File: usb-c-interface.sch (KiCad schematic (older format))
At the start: 62 parts, among them IC3 TPS7A0518PDBVT, J11 12401598E4_2A, J3 12401598E4_2A, J4 12401598E4_2A, U5 TPS25820DSST, U6 NX3DV42GU, U7 TXB0104RUT, U8 CBTL02043ABQ,115, U9 FT232RQ-REEL

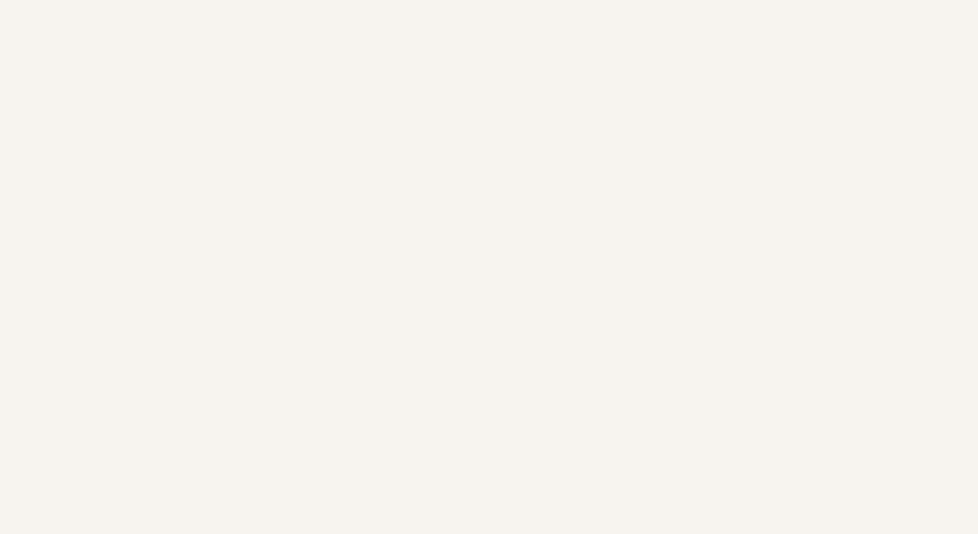
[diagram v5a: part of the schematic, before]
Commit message: Add EDS for host USB-C
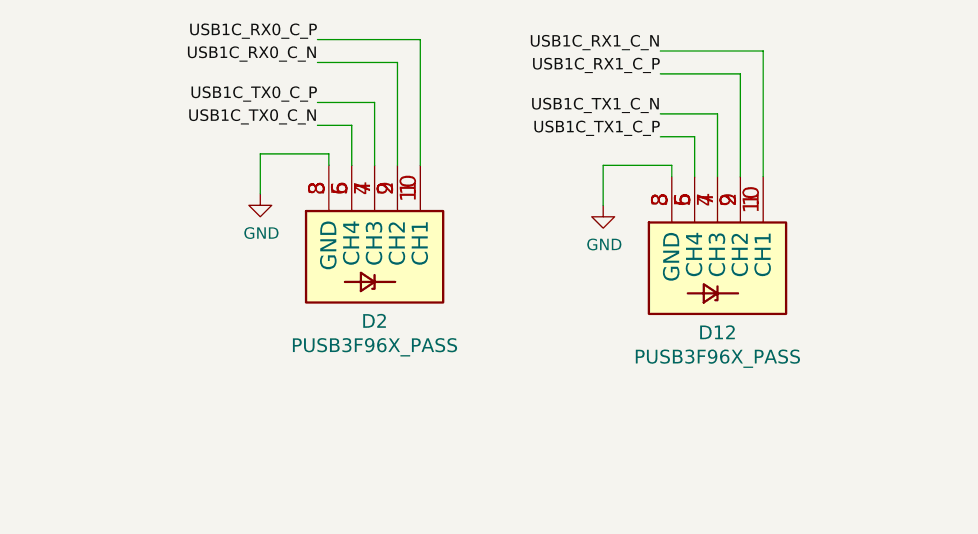
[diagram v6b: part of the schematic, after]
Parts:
- added D12, D2: PUSB3F96X_PASS, sa800u-baseboard-hw-footprints:PUSB3F96X, symbol sa800u-baseboard-hw:PUSB3F96X_PASS
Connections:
- net GND: now also D12.3 (GND), D12.8 (GND), D2.3 (GND), D2.8 (GND)
- net USB1C_RX0_C_N: now also D2.2 (CH2), D2.9 (CH2)
- net USB1C_RX0_C_P: now also D2.1 (CH1), D2.10 (CH1)
- net USB1C_RX1_C_N: now also D12.1 (CH1), D12.10 (CH1)
- net USB1C_RX1_C_P: now also D12.2 (CH2), D12.9 (CH2)
- net USB1C_TX0_C_N: now also D2.5 (CH4), D2.6 (CH4)
- net USB1C_TX0_C_P: now also D2.4 (CH3), D2.7 (CH3)
- net USB1C_TX1_C_N: now also D12.4 (CH3), D12.7 (CH3)
- net USB1C_TX1_C_P: now also D12.5 (CH4), D12.6 (CH4)
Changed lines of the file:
@@
 Text GLabel 1150 9550 0    50   Input ~ 0
 USB2_SS_RX_P
+Wire Wire Line
+	9175 -1675 9175 -1725
+Wire Wire Line
+	8875 -1725 8875 -1550
+$Comp
+L sa800u-baseboard-hw:GND #PWR?
+U 1 1 6217AF63
+P 8875 -1550
+AR Path="/61A60486/6217AF63" Ref="#PWR?"  Part="1"
+AR Path="/61C01D88/6217AF63" Ref="#PWR?"  Part="1"
+AR Path="/61A2F307/6217AF63" Ref="#PWR0257"  Part="1"
+F 0 "#PWR0257" H 8875 -1800 50  0001 C CNN
+F 1 "GND" H 8880 -1723 50  0000 C CNN
+F 2 "" H 8875 -1550 50  0001 C CNN
+F 3 "" H 8875 -1550 50  0001 C CNN
+	1    8875 -1550
+	1    0    0    -1
+$EndComp
+Wire Wire Line
+	9125 -1850 9275 -1850
+Wire Wire Line
+	9275 -1850 9275 -1675
+Wire Wire Line
+	9125 -1950 9375 -1950
+Wire Wire Line
+	9375 -1950 9375 -1675
+Wire Wire Line
+	9475 -1675 9475 -2125
+Wire Wire Line
+	9575 -1675 9575 -2225
+Wire Wire Line
+	8875 -1725 9175 -1725
+$Comp
+L sa800u-baseboard-hw:PUSB3F96X_PASS D?
+U 1 1 6217AF74
+P 9375 -1475
+AR Path="/6197686D/6217AF74" Ref="D?"  Part="1"
+AR Path="/61A2F307/6217AF74" Ref="D12"  Part="1"
+F 0 "D12" V 9858 -1475 60  0000 C CNN
+F 1 "PUSB3F96X_PASS" V 9964 -1475 60  0000 C CNN
+F 2 "sa800u-baseboard-hw-footprints:PUSB3F96X" H 9575 -2025 60  0001 C CNN
+F 3 "https://pl.mouser.com/datasheet/2/916/PUSB3F96-1600324.pdf" H 9375 -1475 60  0001 C CNN
+F 4 "Nexperia" H 9575 -2125 50  0001 C CNN "Manufacturer"
+F 5 "PUSB3F96X" H 9575 -2125 50  0001 C CNN "MPN"
+	1    9375 -1475
+	0    1    1    0
+$EndComp
+Wire Wire Line
+	7675 -1725 7675 -1775
+Wire Wire Line
+	7375 -1775 7375 -1600
+$Comp
+L sa800u-baseboard-hw:GND #PWR?
+U 1 1 621C0750
+P 7375 -1600
+AR Path="/61A60486/621C0750" Ref="#PWR?"  Part="1"
+AR Path="/61C01D88/621C0750" Ref="#PWR?"  Part="1"
+AR Path="/61A2F307/621C0750" Ref="#PWR0265"  Part="1"
+F 0 "#PWR0265" H 7375 -1850 50  0001 C CNN
+F 1 "GND" H 7380 -1773 50  0000 C CNN
+F 2 "" H 7375 -1600 50  0001 C CNN
+F 3 "" H 7375 -1600 50  0001 C CNN
+	1    7375 -1600
+	1    0    0    -1
+$EndComp
+Wire Wire Line
+	7625 -1900 7775 -1900
+Wire Wire Line
+	7775 -1900 7775 -1725
+Wire Wire Line
+	7625 -2000 7875 -2000
+Wire Wire Line
+	7875 -2000 7875 -1725
+Wire Wire Line
+	7975 -1725 7975 -2175
+Wire Wire Line
+	7625 -2175 7975 -2175
+Wire Wire Line
+	8075 -1725 8075 -2275
+Wire Wire Line
+	7625 -2275 8075 -2275
+Wire Wire Line
+	7375 -1775 7675 -1775
+$Comp
+L sa800u-baseboard-hw:PUSB3F96X_PASS D?
+U 1 1 621C0761
+P 7875 -1525
+AR Path="/6197686D/621C0761" Ref="D?"  Part="1"
+AR Path="/61A2F307/621C0761" Ref="D2"  Part="1"
+F 0 "D2" V 8358 -1525 60  0000 C CNN
+F 1 "PUSB3F96X_PASS" V 8464 -1525 60  0000 C CNN
+F 2 "sa800u-baseboard-hw-footprints:PUSB3F96X" H 8075 -2075 60  0001 C CNN
+F 3 "https://pl.mouser.com/datasheet/2/916/PUSB3F96-1600324.pdf" H 7875 -1525 60  0001 C CNN
+F 4 "Nexperia" H 8075 -2175 50  0001 C CNN "Manufacturer"
+F 5 "PUSB3F96X" H 8075 -2175 50  0001 C CNN "MPN"
+	1    7875 -1525
+	0    1    1    0
+$EndComp
+Text Label 7625 -2000 2    50   ~ 0
+USB1C_TX0_C_P
+Text Label 7625 -1900 2    50   ~ 0
+USB1C_TX0_C_N
+Text Label 9125 -2225 2    50   ~ 0
+USB1C_RX1_C_N
+Text Label 9125 -2125 2    50   ~ 0
+USB1C_RX1_C_P
+Text Label 7625 -2275 2    50   ~ 0
+USB1C_RX0_C_P
+Text Label 9125 -1950 2    50   ~ 0
+USB1C_TX1_C_N
+Text Label 9125 -1850 2    50   ~ 0
+USB1C_TX1_C_P
+Text Label 7625 -2175 2    50   ~ 0
+USB1C_RX0_C_N
+Wire Wire Line
+	9125 -2225 9575 -2225
+Wire Wire Line
+	9125 -2125 9475 -2125
 $EndSCHEMATC

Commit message: Continue layout
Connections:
- net USB2C_RX1_N: now also U8.18 (B0_N); no longer U8.16 (B1_N)
- net USB2C_RX1_P: now also U8.19 (B0_P); no longer U8.17 (B1_P)
- net USB2C_RX2_N: now also U8.14 (C0_N); no longer U8.12 (C1_N)
- net USB2C_RX2_P: now also U8.15 (C0_P); no longer U8.13 (C1_P)
- net USB2C_TX1_N: now also U8.16 (B1_N); no longer U8.18 (B0_N)
- net USB2C_TX1_P: now also U8.17 (B1_P); no longer U8.19 (B0_P)
- net USB2C_TX2_N: now also U8.12 (C1_N); no longer U8.14 (C0_N)
- net USB2C_TX2_P: now also U8.13 (C1_P); no longer U8.15 (C0_P)
- net USB2_SS_RX_N: now also U8.4 (A0_N); no longer U8.8 (A1_N)
- net USB2_SS_RX_P: now also U8.3 (A0_P); no longer U8.7 (A1_P)
- net USB2_SS_TX_N: now also U8.8 (A1_N); no longer U8.4 (A0_N)
- net USB2_SS_TX_P: now also U8.7 (A1_P); no longer U8.3 (A0_P)
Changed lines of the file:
@@
 Wire Wire Line
 	2875 2075 3450 2075
-Text Label 3000 10250 2    50   ~ 0
+Text Label 3000 9950 2    50   ~ 0
 USB2C_RX2_N
-Text Label 3000 10150 2    50   ~ 0
+Text Label 3000 9850 2    50   ~ 0
 USB2C_RX2_P
 Wire Wire Line
+	2450 9950 3000 9950
+Wire Wire Line
+	2450 9850 3000 9850
+Wire Wire Line
 	2450 10250 3000 10250
 Wire Wire Line
-	2450 10150 3000 10150
-Wire Wire Line
-	2450 9850 3000 9850
-Wire Wire Line
-	2450 9950 3000 9950
-Text Label 3000 9850 2    50   ~ 0
-USB2C_TX2_P
-Text Label 3000 9950 2    50   ~ 0
-USB2C_TX2_N
+	2450 9350 3000 9350
+Wire Wire Line
+	2450 9450 3000 9450
+Text Label 3000 9350 2    50   ~ 0
+USB2C_TX1_P
+Text Label 3000 9450 2    50   ~ 0
+USB2C_TX1_N
 Wire Wire Line
 	2450 9050 3000 9050
@@
 	2450 9150 3000 9150
 Text Label 3000 9050 2    50   ~ 0
-USB2C_TX1_P
+USB2C_RX1_P
 Text Label 3000 9150 2    50   ~ 0
-USB2C_TX1_N
-Wire Wire Line
-	2450 9350 3000 9350
-Wire Wire Line
-	2450 9450 3000 9450
-Text Label 3000 9350 2    50   ~ 0
-USB2C_RX1_P
-Text Label 3000 9450 2    50   ~ 0
 USB2C_RX1_N
-Text GLabel 1150 9350 0    50   Output ~ 0
+Text GLabel 1150 9650 0    50   Output ~ 0
 USB2_SS_TX_N
-Text GLabel 1150 9250 0    50   Output ~ 0
+Text GLabel 1150 9550 0    50   Output ~ 0
 USB2_SS_TX_P
 $Comp
@@
 Text Label 5600 6900 0    50   ~ 0
 USB2_5V
-Text GLabel 1150 9650 0    50   Input ~ 0
+Text GLabel 1150 9350 0    50   Input ~ 0
 USB2_SS_RX_N
-Text GLabel 1150 9550 0    50   Input ~ 0
+Text GLabel 1150 9250 0    50   Input ~ 0
 USB2_SS_RX_P
 Wire Wire Line
@@
 Wire Wire Line
 	9125 -2125 9475 -2125
+Text Label 3000 10250 2    50   ~ 0
+USB2C_TX2_N
+Text Label 3000 10150 2    50   ~ 0
+USB2C_TX2_P
+Wire Wire Line
+	2450 10150 3000 10150
 $EndSCHEMATC

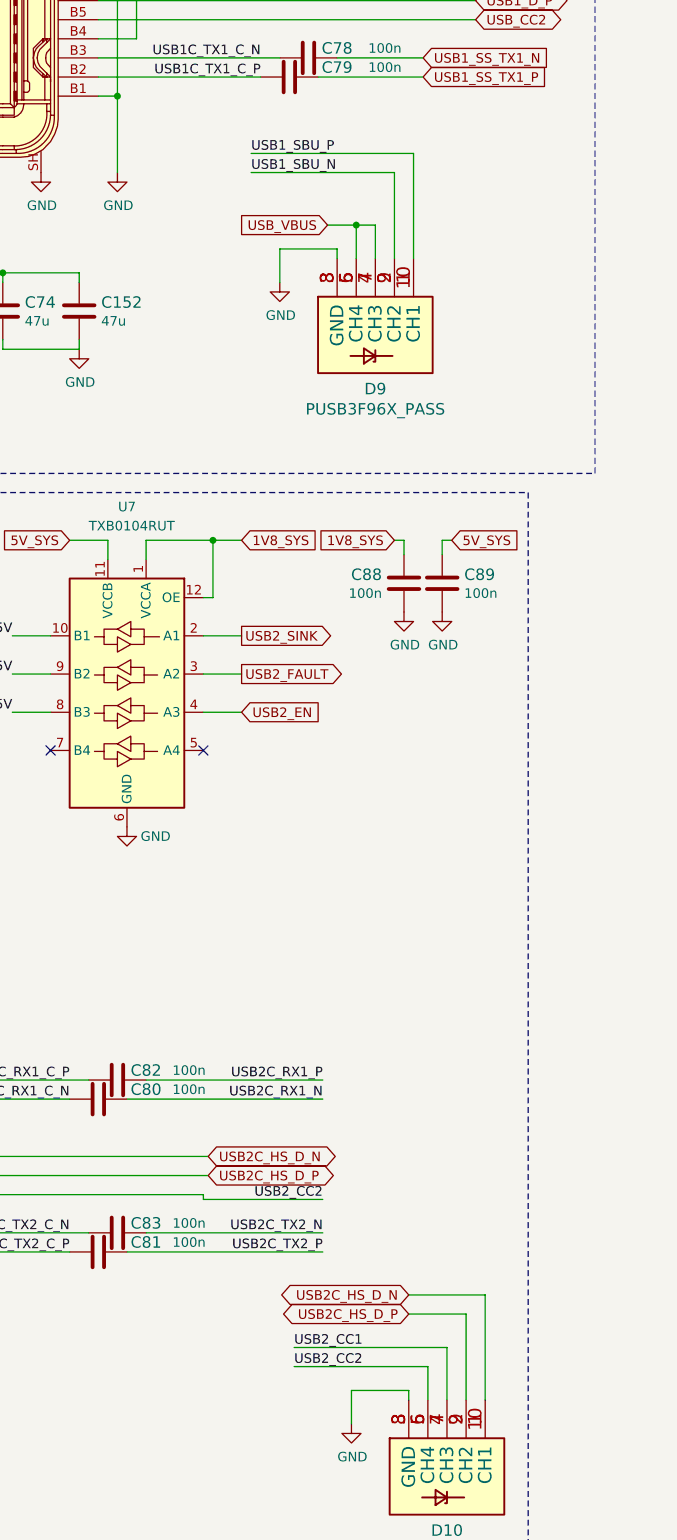
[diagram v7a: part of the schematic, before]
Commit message: Modify TSVs connections
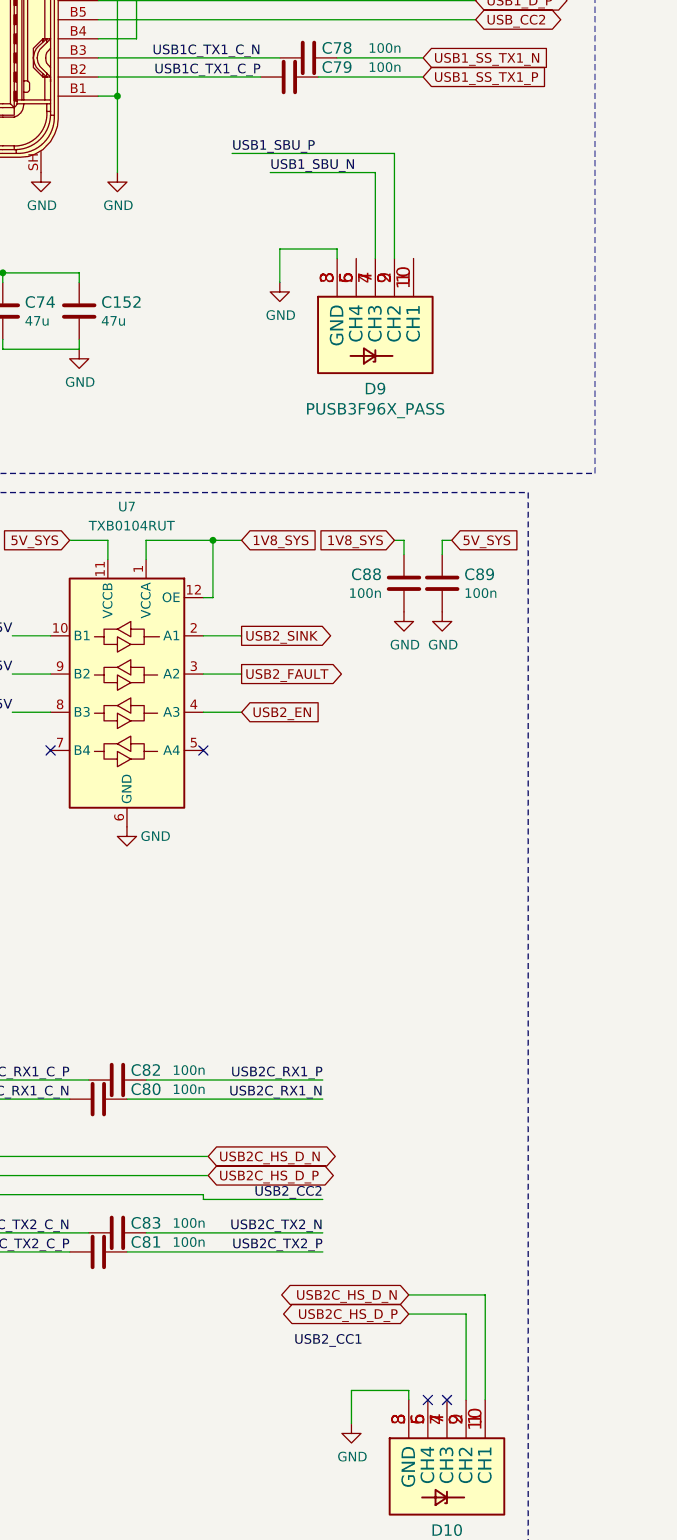
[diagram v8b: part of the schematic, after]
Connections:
- net USB1_SBU_N: now also D9.4 (CH3), D9.7 (CH3); no longer D9.2 (CH2), D9.9 (CH2)
- net USB1_SBU_P: now also D9.2 (CH2), D9.9 (CH2); no longer D9.1 (CH1), D9.10 (CH1)
- net USB2_CC1: no longer D10.4 (CH3), D10.7 (CH3)
- net USB2_CC2: no longer D10.5 (CH4), D10.6 (CH4)
- net USB_VBUS: no longer D9.4 (CH3), D9.5 (CH4), D9.6 (CH4), D9.7 (CH3)
- new net: D10.4 (CH3), D10.7 (CH3)
- new net: D10.5 (CH4), D10.6 (CH4)
- new net: D9.1 (CH1), D9.10 (CH1)
- new net: D9.5 (CH4), D9.6 (CH4)
- no-connect marks 30 -> 32
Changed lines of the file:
@@
 	6775 3225 7175 3225
-Wire Wire Line
-	10325 9575 10325 9750
 Wire Wire Line
 	10225 9300 10525 9300
@@
 Text GLabel 10300 1925 2    50   Input ~ 0
 USB1_SS_RX0_P
-Wire Wire Line
-	10425 9475 10425 9750
 Wire Wire Line
 	7400 2125 7400 1475
@@
 $EndComp
 Wire Wire Line
-	9800 3600 9950 3600
-Wire Wire Line
-	9950 3600 9950 3775
-Wire Wire Line
-	10150 3775 10150 3325
-Wire Wire Line
-	10250 3775 10250 3225
-Text GLabel 9800 3600 0    50   Input ~ 0
-USB_VBUS
-Wire Wire Line
-	9950 3600 10050 3600
-Connection ~ 9950 3600
-Wire Wire Line
-	10050 3600 10050 3775
-Wire Wire Line
-	9400 3325 10150 3325
-Wire Wire Line
-	9400 3225 10250 3225
+	10050 3775 10050 3325
+Wire Wire Line
+	10150 3775 10150 3225
+Wire Wire Line
+	9500 3325 10050 3325
+Wire Wire Line
+	9300 3225 10150 3225
 Text GLabel 4100 2250 2    50   Input ~ 0
 VREG_S4A_1V8
@@
 Text Label 9625 9475 0    50   ~ 0
 USB2_CC1
-Text Label 9625 9575 0    50   ~ 0
-USB2_CC2
-Wire Wire Line
-	9625 9475 10425 9475
-Wire Wire Line
-	9625 9575 10325 9575
 Wire Wire Line
 	13800 8000 14125 8000
@@
 Text Label 4550 3050 2    50   ~ 0
 USB1_SBU_P
-Text Label 9400 3225 0    50   ~ 0
+Text Label 9300 3225 0    50   ~ 0
 USB1_SBU_P
-Text Label 9400 3325 0    50   ~ 0
+Text Label 9500 3325 0    50   ~ 0
 USB1_SBU_N
 Text GLabel 6725 3500 0    50   BiDi ~ 0
@@
 Wire Wire Line
 	2450 10150 3000 10150
+NoConn ~ 10325 9750
+NoConn ~ 10425 9750
 $EndSCHEMATC
